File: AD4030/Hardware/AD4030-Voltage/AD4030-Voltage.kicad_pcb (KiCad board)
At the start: 4 copper layers, 110 x 70 mm, 192 parts, among them J201 1710072, J401 Conn_01x08, J402 Conn_01x07, J403 PMOD, J404 PMOD, J501 1715721, K201 UMS05-1A80-75D, Q201 MMBT3904, Q501 SI5618A, Q502 MMBT3904, U201 ADG1436YCPZ, U202 ADA4817-1ACP, U203 ADA4817-1ACP, U204 TXB0101DBV, U205 LMH6611MK, U206 LMH6611MK, U207 TXB0101DBV, U301 AD8475ACPZ, U302 SN74AUC1G79DBVR, U303 AD4030-24, U304 LTC6655BHMS8-4.096, U401 ADuM260N, U402 ADuM260N, U501 TPS65133DPDR, U502 TSR_1-2433, U503 TEC3-2419WI, U504 LT1763CDE-ADJ, U505 LT1763CDE-1.8, U506 LT1763IDE-3.3, U507 TSR_1-2450, X301 ECS-2520MV-1000-BN-TR

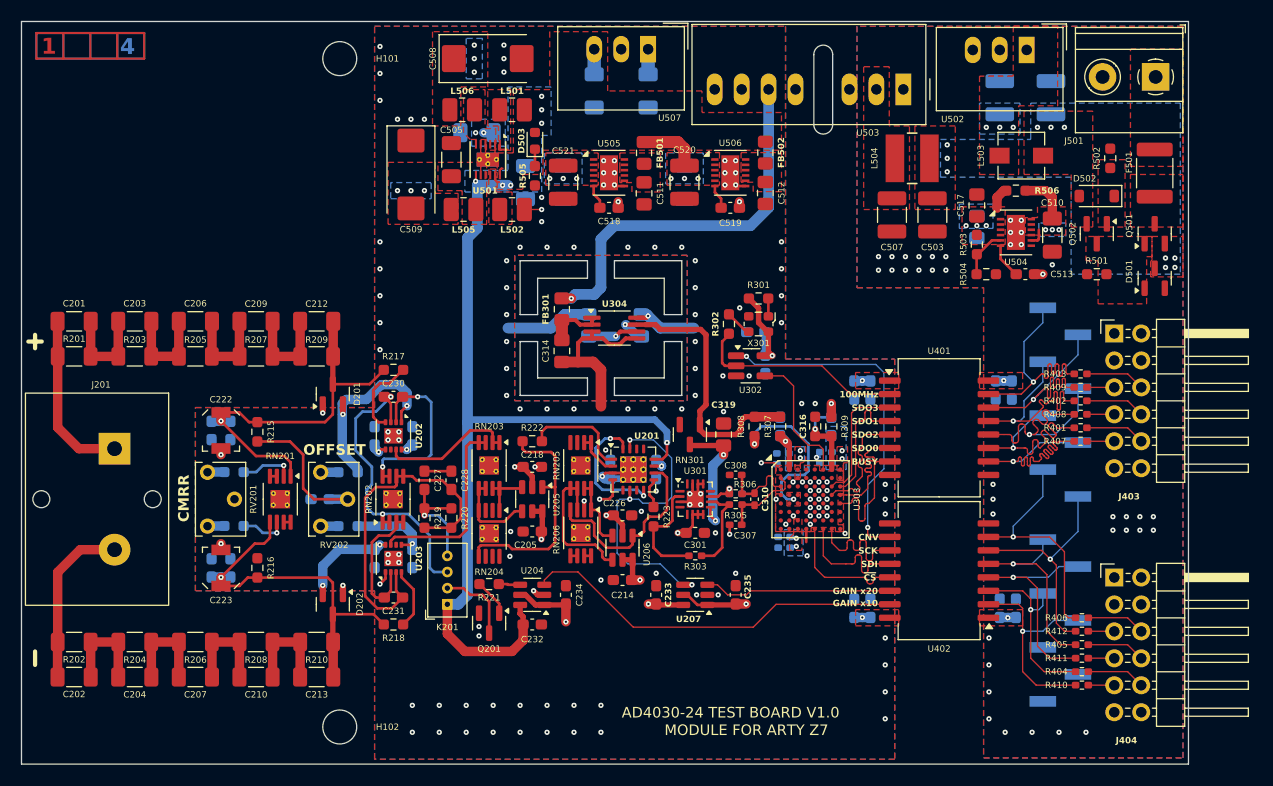
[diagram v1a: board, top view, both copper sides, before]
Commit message: AD4030-Voltage : Ordered BOM
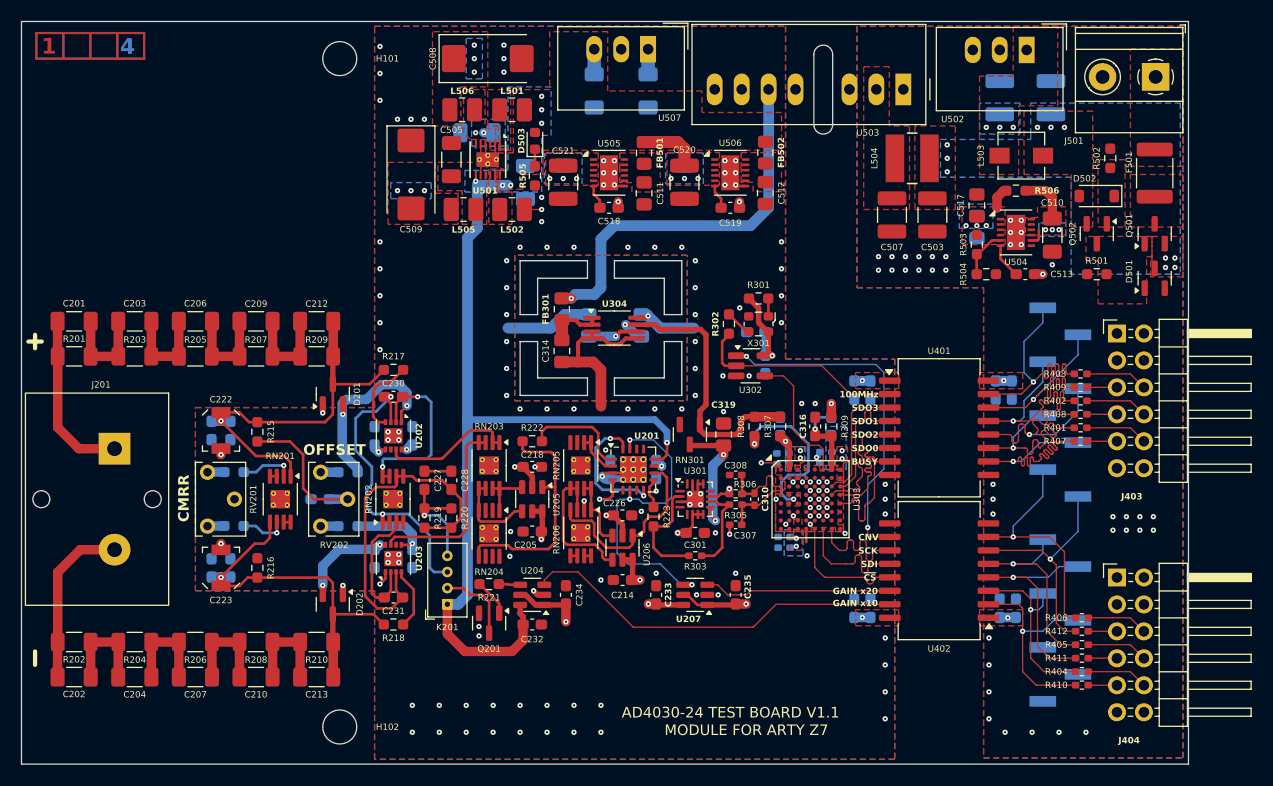
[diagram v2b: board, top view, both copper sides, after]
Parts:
- C316: footprint Resistor_SMD:R_0603_1608Metric_Pad0.98x0.95mm_HandSolder -> Capacitor_SMD:C_0603_1608Metric_Pad1.08x0.95mm_HandSolder
- C510: value 10u -> 10u/25V
- R401, R402, R403, R404, R405, R406, R407, R408, R409, R410, R411, R412: value 50 -> 51
- moved J403 0.25 mm to (183.3, 89.4)
- moved J404 0.25 mm to (183.3, 112.4)
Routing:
- net Net-(J404-Pin_7): track 2.46 -> 2.96 mm
- net Net-(J404-Pin_5): track 2.46 -> 2.96 mm
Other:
- board text added: "AD4030-24 TEST BOARD V1.1"
- board text removed: "AD4030-24 TEST BOARD V1.0"

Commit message: AD4030-Voltage : Fixed model names for reference voltage and isolation ICs.
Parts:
- U304: value LTC6655BHMS8-4.096 -> LTC6655LNBHMS8-4.096
- U401, U402: value ADuM260N -> ADuM260N1
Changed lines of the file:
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@@
 			)
 		)
-		(property "Value" "ADuM260N"
+		(property "Value" "ADuM260N1"
 			(at 0 7.35 0)
 			(layer "F.Fab")
@@
 			)
 		)
-		(property "Value" "LTC6655BHMS8-4.096"
+		(property "Value" "LTC6655LNBHMS8-4.096"
 			(at 0 2.45 0)
 			(layer "F.Fab")
@@
 			)
 		)
-		(property "Value" "ADuM260N"
+		(property "Value" "ADuM260N1"
 			(at 0 7.35 0)
 			(layer "F.Fab")
@@
 	)
 	(zone
+		(net 4)
+		(net_name "Net-(J201-Pin_2)")
+		(layer "F.Cu")
+		(name "$teardrop_padvia$")
+		(hatch full 0.1)
+		(priority 30000)
+		(attr
+			(teardrop
+				(type padvia)
+			)
+		)
+		(connect_pads yes
+			(clearance 0)
+		)
+		(min_thickness 0.0254)
+		(filled_areas_thickness no)
+		(fill yes
+			(thermal_gap 0.5)
+			(thermal_bridge_width 0.5)
+			(island_removal_mode 1)
+			(island_area_min 10)
+		)
+		(polygon
+			(pts
+				(xy 86.273 109.3445) (xy 86.273 110.2335) (xy 87.677797 110.789) (xy 88.774 109.789) (xy 87.677797 108.789)
+			)
+		)
+	)
+	(zone
 		(net 31)
 		(net_name "Net-(J501-Pin_1)")
@@
 	)
 	(zone
-		(net 7)
-		(net_name "GND")
-		(layer "F.Cu")
-		(name "$teardrop_padvia$")
-		(hatch full 0.1)
-		(priority 30021)
-		(attr
-			(teardrop
-				(type padvia)
-			)
-		)
-		(connect_pads yes
-			(clearance 0)
-		)
-		(min_thickness 0.0254)
-		(filled_areas_thickness no)
-		(fill yes
-			(thermal_gap 0.5)
-			(thermal_bridge_width 0.5)
-			(island_removal_mode 1)
-			(island_area_min 10)
-		)
-		(polygon
-			(pts
-				(xy 138.632358 87.7345) (xy 138.632358 88.1155) (xy 139.160671 87.98797) (xy 139.066 87.757) (xy 138.969329 87.52603)
-			)
-		)
-	)
-	(zone
-		(net 2)
-		(net_name "Net-(J201-Pin_1)")
+		(net 151)
+		(net_name "Net-(J403-Pin_7)")
 		(layer "F.Cu")
 		(name "$teardrop_padvia$")
 		(hatch full 0.1)
-		(priority 30001)
+		(priority 30008)
 		(attr
 			(teardrop
@@
 		(polygon
 			(pts
-				(xy 86.273 99.8245) (xy 86.273 100.7135) (xy 87.273 101.269) (xy 88.774 100.269) (xy 87.273 99.269)
+				(xy 181.561 96.9645) (xy 181.561 97.0915) (xy 182.935719 97.813298) (xy 183.262 97.028) (xy 182.935719 96.242702)
 			)
 		)
 	)
 	(zone
-		(net 151)
-		(net_name "Net-(J403-Pin_7)")
+		(net 76)
+		(net_name "/Isolation/CONN_BUSY")
 		(layer "F.Cu")
 		(name "$teardrop_padvia$")
 		(hatch full 0.1)
-		(priority 30008)
+		(priority 30074)
 		(attr
 			(teardrop
@@
 		(polygon
 			(pts
-				(xy 181.561 96.9645) (xy 181.561 97.0915) (xy 182.935719 97.813298) (xy 183.262 97.028) (xy 182.935719 96.242702)
+				(xy 173.999377 101.474135) (xy 173.889393 101.410635) (xy 173.577671 101.24203) (xy 173.4815 101.473866)
+				(xy 173.577671 101.70397)
 			)
 		)
 	)
 	(zone
-		(net 76)
-		(net_name "/Isolation/CONN_BUSY")
+		(net 15)
+		(net_name "-5VA")
 		(layer "F.Cu")
 		(name "$teardrop_padvia$")
 		(hatch full 0.1)
-		(priority 30074)
+		(priority 30044)
 		(attr
 			(teardrop
@@
 		(polygon
 			(pts
-				(xy 173.999377 101.474135) (xy 173.889393 101.410635) (xy 173.577671 101.24203) (xy 173.4815 101.473866)
-				(xy 173.577671 101.70397)
+				(xy 114.067039 100.4745) (xy 114.067039 100.2205) (xy 113.569329 100.35303) (xy 113.664 100.584)
+				(xy 113.841777 100.760777)
 			)
 		)
 	)
 	(zone
-		(net 15)
-		(net_name "-5VA")
+		(net 156)
+		(net_name "Net-(J404-Pin_10)")
 		(layer "F.Cu")
 		(name "$teardrop_padvia$")
 		(hatch full 0.1)
-		(priority 30044)
+		(priority 30004)
 		(attr
 			(teardrop
@@
 		(polygon
 			(pts
-				(xy 114.067039 100.4745) (xy 114.067039 100.2205) (xy 113.569329 100.35303) (xy 113.664 100.584)
-				(xy 113.841777 100.760777)
+				(xy 184.64382 121.321017) (xy 184.554017 121.41082) (xy 185.015702 122.893281) (xy 185.801707 122.568707)
+				(xy 186.126281 121.782702)
 			)
 		)
 	)
 	(zone
-		(net 156)
-		(net_name "Net-(J404-Pin_10)")
+		(net 2)
+		(net_name "Net-(J201-Pin_1)")
 		(layer "F.Cu")
 		(name "$teardrop_padvia$")
 		(hatch full 0.1)
-		(priority 30004)
+		(priority 30001)
 		(attr
 			(teardrop
@@
 		(polygon
 			(pts
-				(xy 184.64382 121.321017) (xy 184.554017 121.41082) (xy 185.015702 122.893281) (xy 185.801707 122.568707)
-				(xy 186.126281 121.782702)
+				(xy 86.273 99.8245) (xy 86.273 100.7135) (xy 87.273 101.269) (xy 88.774 100.269) (xy 87.273 99.269)
 			)
 		)
@@
 	)
 	(zone
+		(net 15)
+		(net_name "-5VA")
+		(layer "F.Cu")
+		(name "$teardrop_padvia$")
+		(hatch full 0.1)
+		(priority 30002)
+		(attr
+			(teardrop
+				(type padvia)
+			)
+		)
+		(connect_pads yes
+			(clearance 0)
+		)
+		(min_thickness 0.0254)
+		(filled_areas_thickness no)
+		(fill yes
+			(thermal_gap 0.5)
+			(thermal_bridge_width 0.5)
+			(island_removal_mode 1)
+			(island_area_min 10)
+		)
+		(polygon
+			(pts
+				(xy 137.202619 102.433) (xy 137.202619 102.687) (xy 137.782805 102.512164) (xy 137.669 102.235)
+				(xy 137.390836 102.120195)
+			)
+		)
+	)
+	(zone
 		(net 152)
 		(net_name "Net-(J403-Pin_9)")
@@
 	)
 	(zone
-		(net 51)
-		(net_name "VDDF")
-		(layer "F.Cu")
-		(name "$teardrop_padvia$")
-		(hatch full 0.1)
-		(priority 30018)
-		(attr
-			(teardrop
-				(type padvia)
-			)
-		)
-		(connect_pads yes
-			(clearance 0)
-		)
-		(min_thickness 0.0254)
-		(filled_areas_thickness no)
-		(fill yes
-			(thermal_gap 0.5)
-			(thermal_bridge_width 0.5)
-			(island_removal_mode 1)
-			(island_area_min 10)
-		)
-		(polygon
-			(pts
-				(xy 137.406 88.7655) (xy 137.406 88.3845) (xy 136.906 88.325) (xy 136.905 88.575) (xy 136.906 88.825)
-			)
-		)
-	)
-	(zone
 		(net 43)
 		(net_name "Net-(U202-FB)")
@@
 	)
 	(zone
-		(net 15)
-		(net_name "-5VA")
-		(layer "F.Cu")
-		(name "$teardrop_padvia$")
-		(hatch full 0.1)
-		(priority 30002)
-		(attr
-			(teardrop
-				(type padvia)
-			)
-		)
-		(connect_pads yes
-			(clearance 0)
-		)
-		(min_thickness 0.0254)
-		(filled_areas_thickness no)
-		(fill yes
-			(thermal_gap 0.5)
-			(thermal_bridge_width 0.5)
-			(island_removal_mode 1)
-			(island_area_min 10)
-		)
-		(polygon
-			(pts
-				(xy 137.202619 102.433) (xy 137.202619 102.687) (xy 137.782805 102.512164) (xy 137.669 102.235)
-				(xy 137.390836 102.120195)
-			)
-		)
-	)
-	(zone
 		(net 159)
 		(net_name "Net-(J404-Pin_9)")
@@
 			)
 		)
-	)
-	(zone
-		(net 4)
-		(net_name "Net-(J201-Pin_2)")
-		(layer "F.Cu")
-		(name "$teardrop_padvia$")
-		(hatch full 0.1)
-		(priority 30000)
-		(attr
-			(teardrop
-				(type padvia)
-			)
-		)
-		(connect_pads yes
-			(clearance 0)
-		)
-		(min_thickness 0.0254)
-		(filled_areas_thickness no)
-		(fill yes
-			(thermal_gap 0.5)
-			(thermal_bridge_width 0.5)
-			(island_removal_mode 1)
-			(island_area_min 10)
-		)
-		(polygon
-			(pts
-				(xy 86.273 109.3445) (xy 86.273 110.2335) (xy 87.677797 110.789) (xy 88.774 109.789) (xy 87.677797 108.789)
-			)
-		)

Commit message: Software tests
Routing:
- net GND: track 57.6 -> 75.2 mm
- net +1V8: track 27.6 -> 31.2 mm
- net Net-(U303-~{RST}): track 7.83 -> 10.9 mm
- net Net-(R308-Pad2): track 15.8 -> 18.1 mm
- net +5VA: track 48.2 -> 50.2 mm
- net Net-(U303-REFIN): track 5.22 -> 4.26 mm
- removed copper zone on F.Cu, net Net-(R308-Pad2)
